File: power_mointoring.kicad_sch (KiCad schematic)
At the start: 19 parts, among them J10 BATT out, J11 Vin, J7 VCC, J8 Servo pwr, J9 BATT in, SW5 POWER, U3 3V3 REG, U4 DS2438Z+, U5 DS2438Z+

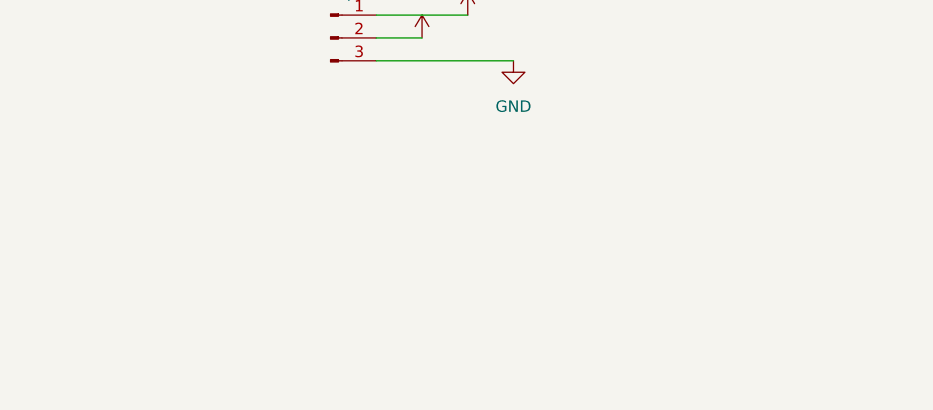
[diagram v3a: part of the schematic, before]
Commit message: Added revision 2 features, not routed.
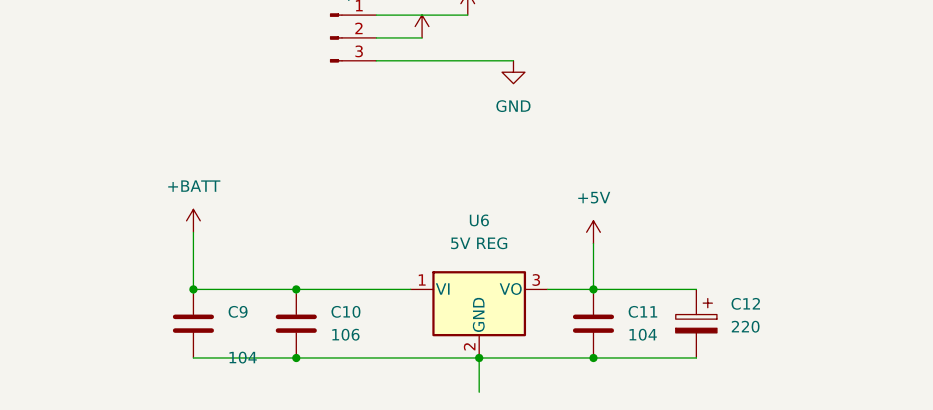
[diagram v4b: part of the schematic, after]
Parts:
- added C10: 106, Capacitor_SMD:C_1210_3225Metric_Pad1.33x2.70mm_HandSolder, symbol Device:C
- added C11, C9: 104, Capacitor_SMD:C_1206_3216Metric_Pad1.33x1.80mm_HandSolder, symbol Device:C
- added C12: 220, Capacitor_SMD:C_Elec_6.3x5.8, symbol Device:C_Polarized
- added U6: 5V REG, Package_TO_SOT_THT:TO-220-3_Vertical, symbol Regulator_Linear:LT1584-3.3
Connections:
- net +5V: now also C11.1, C12.1, U6.3 (VO)
- net +BATT: now also C10.1, C9.1, U6.1 (VI)
- new net: C10.2, C11.2, C12.2, C9.2, U6.2 (GND)
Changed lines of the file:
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@@
     (company "James Hudson")
   )
+  (junction (at 66.04 180.34) (diameter 0) (color 0 0 0 0)
+  )
   (junction (at 111.76 92.71) (diameter 0) (color 0 0 0 0)
   )
@@
   (junction (at 44.45 35.56) (diameter 0) (color 0 0 0 0)
   )
+  (junction (at 77.47 187.96) (diameter 0) (color 0 0 0 0)
+  )
   (junction (at 77.47 35.56) (diameter 0) (color 0 0 0 0)
   )
+  (junction (at 77.47 180.34) (diameter 0) (color 0 0 0 0)
+  )
+  (junction (at 97.79 187.96) (diameter 0) (color 0 0 0 0)
+  )
+  (junction (at 110.49 187.96) (diameter 0) (color 0 0 0 0)
+  )
   (junction (at 33.02 35.56) (diameter 0) (color 0 0 0 0)
   )
@@
   (junction (at 64.77 43.18) (diameter 0) (color 0 0 0 0)
   )
+  (junction (at 110.49 180.34) (diameter 0) (color 0 0 0 0)
+  )
   (wire (pts (xy 97.79 82.55) (xy 97.79 92.71))
     (stroke (width 0) (type default) (color 0 0 0 0))
@@
     (stroke (width 0) (type default) (color 0 0 0 0))
   )
+  (wire (pts (xy 66.04 173.99) (xy 66.04 180.34))
+    (stroke (width 0) (type default) (color 0 0 0 0))
+  )
+  (wire (pts (xy 97.79 187.96) (xy 97.79 191.77))
+    (stroke (width 0) (type default) (color 0 0 0 0))
+  )
   (wire (pts (xy 194.31 116.84) (xy 199.39 116.84))
     (stroke (width 0) (type default) (color 0 0 0 0))
@@
     (stroke (width 0) (type default) (color 0 0 0 0))
   )
+  (wire (pts (xy 90.17 180.34) (xy 77.47 180.34))
+    (stroke (width 0) (type default) (color 0 0 0 0))
+  )
   (wire (pts (xy 149.86 72.39) (xy 149.86 77.47))
     (stroke (width 0) (type default) (color 0 0 0 0))
   )
+  (wire (pts (xy 110.49 175.26) (xy 110.49 180.34))
+    (stroke (width 0) (type default) (color 0 0 0 0))
+  )
   (wire (pts (xy 137.16 62.23) (xy 161.29 62.23))
     (stroke (width 0) (type default) (color 0 0 0 0))
@@
     (stroke (width 0) (type default) (color 0 0 0 0))
   )
+  (wire (pts (xy 110.49 187.96) (xy 121.92 187.96))
+    (stroke (width 0) (type default) (color 0 0 0 0))
+  )
   (wire (pts (xy 86.36 154.94) (xy 101.6 154.94))
     (stroke (width 0) (type default) (color 0 0 0 0))
@@
     (stroke (width 0) (type default) (color 0 0 0 0))
   )
+  (wire (pts (xy 110.49 180.34) (xy 121.92 180.34))
+    (stroke (width 0) (type default) (color 0 0 0 0))
+  )
   (wire (pts (xy 107.95 69.85) (xy 115.57 69.85))
     (stroke (width 0) (type default) (color 0 0 0 0))
@@
     (stroke (width 0) (type default) (color 0 0 0 0))
   )
+  (wire (pts (xy 105.41 180.34) (xy 110.49 180.34))
+    (stroke (width 0) (type default) (color 0 0 0 0))
+  )
   (wire (pts (xy 161.29 72.39) (xy 161.29 69.85))
     (stroke (width 0) (type default) (color 0 0 0 0))
@@
     (stroke (width 0) (type default) (color 0 0 0 0))
   )
+  (wire (pts (xy 97.79 187.96) (xy 110.49 187.96))
+    (stroke (width 0) (type default) (color 0 0 0 0))
+  )
   (wire (pts (xy 77.47 35.56) (xy 88.9 35.56))
     (stroke (width 0) (type default) (color 0 0 0 0))
@@
     (stroke (width 0) (type default) (color 0 0 0 0))
   )
+  (wire (pts (xy 66.04 180.34) (xy 77.47 180.34))
+    (stroke (width 0) (type default) (color 0 0 0 0))
+  )
   (wire (pts (xy 33.02 43.18) (xy 44.45 43.18))
     (stroke (width 0) (type default) (color 0 0 0 0))
@@
     (stroke (width 0) (type default) (color 0 0 0 0))
   )
+  (wire (pts (xy 77.47 187.96) (xy 97.79 187.96))
+    (stroke (width 0) (type default) (color 0 0 0 0))
+  )
   (wire (pts (xy 161.29 129.54) (xy 144.78 129.54))
     (stroke (width 0) (type default) (color 0 0 0 0))
@@
   )
   (wire (pts (xy 77.47 30.48) (xy 77.47 35.56))
+    (stroke (width 0) (type default) (color 0 0 0 0))
+  )
+  (wire (pts (xy 66.04 187.96) (xy 77.47 187.96))
     (stroke (width 0) (type default) (color 0 0 0 0))
   )
@@
     (pin "2")
     (pin "3")
+  )
+  (symbol (lib_id "Device:C") (at 66.04 184.15 0) (unit 1)
+    (in_bom yes) (on_board yes)
+    (property "Reference" "C9" (id 0) (at 69.85 182.8799 0)
+      (effects (font (size 1.27 1.27)) (justify left))
+    )
+    (property "Value" "104" (id 1) (at 69.85 187.96 0)
+      (effects (font (size 1.27 1.27)) (justify left))
+    )
+    (property "Footprint" "Capacitor_SMD:C_1206_3216Metric_Pad1.33x1.80mm_HandSolder" (id 2) (at 67.0052 187.96 0)
+      (effects (font (size 1.27 1.27)) hide)
+    )
+    (property "Datasheet" "~" (id 3) (at 66.04 184.15 0)
+      (effects (font (size 1.27 1.27)) hide)
+    )
+    (pin "1")
+    (pin "2")
   )
   (symbol (lib_id "Switch:SW_SPDT") (at 120.65 72.39 0) (mirror y) (unit 1)
@@
     (pin "2")
   )
+  (symbol (lib_id "Device:C") (at 77.47 184.15 0) (unit 1)
+    (in_bom yes) (on_board yes) (fields_autoplaced)
+    (property "Reference" "C10" (id 0) (at 81.28 182.8799 0)
+      (effects (font (size 1.27 1.27)) (justify left))
+    )
+    (property "Value" "106" (id 1) (at 81.28 185.4199 0)
+      (effects (font (size 1.27 1.27)) (justify left))
+    )
+    (property "Footprint" "Capacitor_SMD:C_1210_3225Metric_Pad1.33x2.70mm_HandSolder" (id 2) (at 78.4352 187.96 0)
+      (effects (font (size 1.27 1.27)) hide)
+    )
+    (property "Datasheet" "~" (id 3) (at 77.47 184.15 0)
+      (effects (font (size 1.27 1.27)) hide)
+    )
+    (pin "1")
+    (pin "2")
+  )
   (symbol (lib_id "Connector:Conn_01x02_Male") (at 48.26 111.76 0) (unit 1)
     (in_bom yes) (on_board yes) (fields_autoplaced)
@@
     )
     (property "Datasheet" "https://www.analog.com/media/en/technical-documentation/data-sheets/158457a.pdf" (id 3) (at 64.77 57.15 0)
+      (effects (font (size 1.27 1.27)) hide)
+    )
+    (pin "1")
+    (pin "2")
+    (pin "3")
+  )
+  (symbol (lib_id "Regulator_Linear:LT1584-3.3") (at 97.79 180.34 0) (unit 1)
+    (in_bom yes) (on_board yes) (fields_autoplaced)
+    (property "Reference" "U6" (id 0) (at 97.79 172.72 0))
+    (property "Value" "5V REG" (id 1) (at 97.79 175.26 0))
+    (property "Footprint" "Package_TO_SOT_THT:TO-220-3_Vertical" (id 2) (at 97.79 173.99 0)
+      (effects (font (size 1.27 1.27) italic) hide)
+    )
+    (property "Datasheet" "https://www.analog.com/media/en/technical-documentation/data-sheets/158457a.pdf" (id 3) (at 97.79 201.93 0)
       (effects (font (size 1.27 1.27)) hide)
     )
@@
     (pin "8")
   )
+  (symbol (lib_id "power:+BATT") (at 66.04 173.99 0) (unit 1)
+    (in_bom yes) (on_board yes) (fields_autoplaced)
+    (property "Reference" "#PWR0115" (id 0) (at 66.04 177.8 0)
+      (effects (font (size 1.27 1.27)) hide)
+    )
+    (property "Value" "+BATT" (id 1) (at 66.04 168.91 0))
+    (property "Footprint" "" (id 2) (at 66.04 173.99 0)
+      (effects (font (size 1.27 1.27)) hide)
+    )
+    (property "Datasheet" "" (id 3) (at 66.04 173.99 0)
+      (effects (font (size 1.27 1.27)) hide)
+    )
+    (pin "1")
+  )
   (symbol (lib_id "power:VCC") (at 152.4 116.84 0) (unit 1)
     (in_bom yes) (on_board yes) (fields_autoplaced)
@@
     )
     (property "Datasheet" "" (id 3) (at 152.4 116.84 0)
+      (effects (font (size 1.27 1.27)) hide)
+    )
+    (pin "1")
+  )
+  (symbol (lib_id "Device:C") (at 110.49 184.15 0) (unit 1)
+    (in_bom yes) (on_board yes) (fields_autoplaced)
+    (property "Reference" "C11" (id 0) (at 114.3 182.8799 0)
+      (effects (font (size 1.27 1.27)) (justify left))
+    )
+    (property "Value" "104" (id 1) (at 114.3 185.4199 0)
+      (effects (font (size 1.27 1.27)) (justify left))
+    )
+    (property "Footprint" "Capacitor_SMD:C_1206_3216Metric_Pad1.33x1.80mm_HandSolder" (id 2) (at 111.4552 187.96 0)
+      (effects (font (size 1.27 1.27)) hide)
+    )
+    (property "Datasheet" "~" (id 3) (at 110.49 184.15 0)
+      (effects (font (size 1.27 1.27)) hide)
+    )
+    (pin "1")
+    (pin "2")
+  )
+  (symbol (lib_id "power:+5V") (at 110.49 175.26 0) (unit 1)
+    (in_bom yes) (on_board yes) (fields_autoplaced)
+    (property "Reference" "#PWR0114" (id 0) (at 110.49 179.07 0)
+      (effects (font (size 1.27 1.27)) hide)
+    )
+    (property "Value" "+5V" (id 1) (at 110.49 170.18 0))
+    (property "Footprint" "" (id 2) (at 110.49 175.26 0)
+      (effects (font (size 1.27 1.27)) hide)
+    )
+    (property "Datasheet" "" (id 3) (at 110.49 175.26 0)
       (effects (font (size 1.27 1.27)) hide)
     )
@@
     (pin "1")
   )
+  (symbol (lib_id "Device:C_Polarized") (at 121.92 184.15 0) (mirror y) (unit 1)
+    (in_bom yes) (on_board yes) (fields_autoplaced)
+    (property "Reference" "C12" (id 0) (at 125.73 181.9909 0)
+      (effects (font (size 1.27 1.27)) (justify right))
+    )
+    (property "Value" "220" (id 1) (at 125.73 184.5309 0)
+      (effects (font (size 1.27 1.27)) (justify right))
+    )
+    (property "Footprint" "Capacitor_SMD:C_Elec_6.3x5.8" (id 2) (at 120.9548 187.96 0)
+      (effects (font (size 1.27 1.27)) hide)
+    )
+    (property "Datasheet" "~" (id 3) (at 121.92 184.15 0)
+      (effects (font (size 1.27 1.27)) hide)
+    )
+    (pin "1")
+    (pin "2")
+  )
   (symbol (lib_id "power:+BATT") (at 133.35 72.39 0) (unit 1)

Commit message: Board ready to go.
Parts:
- removed J10: BATT out, Connector_PinHeader_2.54mm:Connector_Battery_SolderPads, symbol Connector:Conn_01x02_Male
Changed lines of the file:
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@@
-    (stroke (width 0) (type default) (color 0 0 0 0))
-  )
-  (wire (pts (xy 99.06 121.92) (xy 104.14 121.92))
     (stroke (width 0) (type default) (color 0 0 0 0))
   )
@@
   )
   (wire (pts (xy 194.31 109.22) (xy 194.31 116.84))
-    (stroke (width 0) (type default) (color 0 0 0 0))
-  )
-  (wire (pts (xy 99.06 119.38) (xy 104.14 119.38))
     (stroke (width 0) (type default) (color 0 0 0 0))
   )
@@
     (pin "2")
   )
-  (symbol (lib_id "power:+BATT") (at 104.14 119.38 0) (unit 1)
-    (in_bom yes) (on_board yes)
-    (property "Reference" "#PWR067" (id 0) (at 104.14 123.19 0)
-      (effects (font (size 1.27 1.27)) hide)
-    )
-    (property "Value" "+BATT" (id 1) (at 104.14 114.3 0))
-    (property "Footprint" "" (id 2) (at 104.14 119.38 0)
-      (effects (font (size 1.27 1.27)) hide)
-    )
-    (property "Datasheet" "" (id 3) (at 104.14 119.38 0)
-      (effects (font (size 1.27 1.27)) hide)
-    )
-    (pin "1")
-  )
   (symbol (lib_id "power:GND") (at 153.67 92.71 0) (unit 1)
     (in_bom yes) (on_board yes) (fields_autoplaced)
@@
     (pin "1")
     (pin "2")
-  )
-  (symbol (lib_id "power:GND") (at 104.14 121.92 0) (unit 1)
-    (in_bom yes) (on_board yes) (fields_autoplaced)
-    (property "Reference" "#PWR068" (id 0) (at 104.14 128.27 0)
-      (effects (font (size 1.27 1.27)) hide)
-    )
-    (property "Value" "GND" (id 1) (at 104.14 127 0))
-    (property "Footprint" "" (id 2) (at 104.14 121.92 0)
-      (effects (font (size 1.27 1.27)) hide)
-    )
-    (property "Datasheet" "" (id 3) (at 104.14 121.92 0)
-      (effects (font (size 1.27 1.27)) hide)
-    )
-    (pin "1")
   )
   (symbol (lib_id "Device:C") (at 77.47 39.37 0) (unit 1)
@@
     (pin "1")
   )
-  (symbol (lib_id "Connector:Conn_01x02_Male") (at 93.98 119.38 0) (unit 1)
-    (in_bom yes) (on_board yes) (fields_autoplaced)
-    (property "Reference" "J10" (id 0) (at 94.615 114.3 0))
-    (property "Value" "BATT out" (id 1) (at 94.615 116.84 0))
-    (property "Footprint" "Connector_PinHeader_2.54mm:Connector_Battery_SolderPads" (id 2) (at 93.98 119.38 0)
-      (effects (font (size 1.27 1.27)) hide)
-    )
-    (property "Datasheet" "~" (id 3) (at 93.98 119.38 0)
-      (effects (font (size 1.27 1.27)) hide)
-    )
-    (pin "1")
-    (pin "2")
-  )
   (symbol (lib_id "Device:R") (at 149.86 81.28 0) (unit 1)

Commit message: Clean chematic
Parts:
- added J10: Servo pwr, Connector_PinHeader_2.54mm:Connector_SolderPadsx3, symbol Connector:Conn_01x03_Male
- added J13: VCC, Connector_PinHeader_2.54mm:PinHeader_1x02_P2.54mm_Vertical, symbol Connector:Conn_01x02_Male
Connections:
- net +5V: no longer U4.4 (VAD)
- net GND: now also J10.3 (Pin_3), J13.2 (Pin_2)
- net VCC: now also J13.1 (Pin_1)
- new net +5VA: J10.1 (Pin_1)
- new net +5VL: J10.2 (Pin_2), U4.4 (VAD)
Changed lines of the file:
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@@
+    (stroke (width 0) (type default) (color 0 0 0 0))
+  )
+  (wire (pts (xy 53.34 132.08) (xy 58.42 132.08))
     (stroke (width 0) (type default) (color 0 0 0 0))
   )
@@
     (stroke (width 0) (type default) (color 0 0 0 0))
   )
+  (wire (pts (xy 133.35 154.94) (xy 148.59 154.94))
+    (stroke (width 0) (type default) (color 0 0 0 0))
+  )
   (wire (pts (xy 97.79 187.96) (xy 97.79 191.77))
     (stroke (width 0) (type default) (color 0 0 0 0))
   )
+  (wire (pts (xy 53.34 134.62) (xy 58.42 134.62))
+    (stroke (width 0) (type default) (color 0 0 0 0))
+  )
   (wire (pts (xy 194.31 116.84) (xy 199.39 116.84))
     (stroke (width 0) (type default) (color 0 0 0 0))
@@
     (stroke (width 0) (type default) (color 0 0 0 0))
   )
+  (wire (pts (xy 133.35 149.86) (xy 143.51 149.86))
+    (stroke (width 0) (type default) (color 0 0 0 0))
+  )
   (wire (pts (xy 189.23 69.85) (xy 189.23 76.2))
     (stroke (width 0) (type default) (color 0 0 0 0))
@@
   )
   (wire (pts (xy 161.29 129.54) (xy 144.78 129.54))
+    (stroke (width 0) (type default) (color 0 0 0 0))
+  )
+  (wire (pts (xy 133.35 152.4) (xy 147.32 152.4))
     (stroke (width 0) (type default) (color 0 0 0 0))
   )
@@
     (pin "2")
   )
+  (symbol (lib_id "power:VCC") (at 58.42 132.08 0) (unit 1)
+    (in_bom yes) (on_board yes) (fields_autoplaced)
+    (property "Reference" "#PWR0178" (id 0) (at 58.42 135.89 0)
+      (effects (font (size 1.27 1.27)) hide)
+    )
+    (property "Value" "VCC" (id 1) (at 58.42 127 0))
+    (property "Footprint" "" (id 2) (at 58.42 132.08 0)
+      (effects (font (size 1.27 1.27)) hide)
+    )
+    (property "Datasheet" "" (id 3) (at 58.42 132.08 0)
+      (effects (font (size 1.27 1.27)) hide)
+    )
+    (pin "1")
+  )
   (symbol (lib_id "Connector:Conn_01x02_Male") (at 92.71 80.01 0) (unit 1)
     (in_bom yes) (on_board yes) (fields_autoplaced)
@@
     (pin "1")
   )
+  (symbol (lib_id "power:GND") (at 58.42 134.62 0) (unit 1)
+    (in_bom yes) (on_board yes) (fields_autoplaced)
+    (property "Reference" "#PWR0176" (id 0) (at 58.42 140.97 0)
+      (effects (font (size 1.27 1.27)) hide)
+    )
+    (property "Value" "GND" (id 1) (at 58.42 139.7 0))
+    (property "Footprint" "" (id 2) (at 58.42 134.62 0)
+      (effects (font (size 1.27 1.27)) hide)
+    )
+    (property "Datasheet" "" (id 3) (at 58.42 134.62 0)
+      (effects (font (size 1.27 1.27)) hide)
+    )
+    (pin "1")
+  )
+  (symbol (lib_id "power:GND") (at 148.59 154.94 0) (unit 1)
+    (in_bom yes) (on_board yes) (fields_autoplaced)
+    (property "Reference" "#PWR0157" (id 0) (at 148.59 161.29 0)
+      (effects (font (size 1.27 1.27)) hide)
+    )
+    (property "Value" "GND" (id 1) (at 148.59 160.02 0))
+    (property "Footprint" "" (id 2) (at 148.59 154.94 0)
+      (effects (font (size 1.27 1.27)) hide)
+    )
+    (property "Datasheet" "" (id 3) (at 148.59 154.94 0)
+      (effects (font (size 1.27 1.27)) hide)
+    )
+    (pin "1")
+  )
   (symbol (lib_id "Device:C") (at 143.51 72.39 270) (unit 1)
     (in_bom yes) (on_board yes) (fields_autoplaced)
@@
     (pin "1")
   )
+  (symbol (lib_id "Connector:Conn_01x02_Male") (at 48.26 132.08 0) (unit 1)
+    (in_bom yes) (on_board yes) (fields_autoplaced)
+    (property "Reference" "J13" (id 0) (at 48.895 127 0))
+    (property "Value" "VCC" (id 1) (at 48.895 129.54 0))
+    (property "Footprint" "Connector_PinHeader_2.54mm:PinHeader_1x02_P2.54mm_Vertical" (id 2) (at 48.26 132.08 0)
+      (effects (font (size 1.27 1.27)) hide)
+    )
+    (property "Datasheet" "~" (id 3) (at 48.26 132.08 0)
+      (effects (font (size 1.27 1.27)) hide)
+    )
+    (pin "1")
+    (pin "2")
+  )
   (symbol (lib_id "Device:Fuse") (at 104.14 69.85 270) (unit 1)
     (in_bom yes) (on_board yes) (fields_autoplaced)
@@
     (pin "1")
     (pin "2")
+  )
+  (symbol (lib_id "power:+5VA") (at 143.51 149.86 0) (unit 1)
+    (in_bom yes) (on_board yes) (fields_autoplaced)
+    (property "Reference" "#PWR0154" (id 0) (at 143.51 153.67 0)
+      (effects (font (size 1.27 1.27)) hide)
+    )
+    (property "Value" "+5VA" (id 1) (at 143.51 144.78 0))
+    (property "Footprint" "" (id 2) (at 143.51 149.86 0)
+      (effects (font (size 1.27 1.27)) hide)
+    )
+    (property "Datasheet" "" (id 3) (at 143.51 149.86 0)
+      (effects (font (size 1.27 1.27)) hide)
+    )
+    (pin "1")
   )
   (symbol (lib_id "Device:C") (at 77.47 39.37 0) (unit 1)
@@
     (pin "1")
   )
-  (symbol (lib_id "power:+5V") (at 156.21 72.39 0) (unit 1)
-    (in_bom yes) (on_board yes) (fields_autoplaced)
-    (property "Reference" "#PWR073" (id 0) (at 156.21 76.2 0)
-      (effects (font (size 1.27 1.27)) hide)
-    )
-    (property "Value" "+5V" (id 1) (at 156.21 67.31 0))
-    (property "Footprint" "" (id 2) (at 156.21 72.39 0)
-      (effects (font (size 1.27 1.27)) hide)
-    )
-    (property "Datasheet" "" (id 3) (at 156.21 72.39 0)
-      (effects (font (size 1.27 1.27)) hide)
-    )
-    (pin "1")
-  )
   (symbol (lib_id "power:+5V") (at 96.52 149.86 0) (unit 1)
     (in_bom yes) (on_board yes) (fields_autoplaced)
@@
     )
     (property "Datasheet" "" (id 3) (at 96.52 149.86 0)
+      (effects (font (size 1.27 1.27)) hide)
+    )
+    (pin "1")
+  )
+  (symbol (lib_id "power:+5VL") (at 147.32 152.4 0) (unit 1)
+    (in_bom yes) (on_board yes) (fields_autoplaced)
+    (property "Reference" "#PWR0166" (id 0) (at 147.32 156.21 0)
+      (effects (font (size 1.27 1.27)) hide)
+    )
+    (property "Value" "+5VL" (id 1) (at 147.32 147.32 0))
+    (property "Footprint" "" (id 2) (at 147.32 152.4 0)
+      (effects (font (size 1.27 1.27)) hide)
+    )
+    (property "Datasheet" "" (id 3) (at 147.32 152.4 0)
+      (effects (font (size 1.27 1.27)) hide)
+    )
+    (pin "1")
+  )
+  (symbol (lib_id "power:+5VL") (at 156.21 72.39 0) (unit 1)
+    (in_bom yes) (on_board yes) (fields_autoplaced)
+    (property "Reference" "#PWR0172" (id 0) (at 156.21 76.2 0)
+      (effects (font (size 1.27 1.27)) hide)
+    )
+    (property "Value" "+5VL" (id 1) (at 156.21 67.31 0))
+    (property "Footprint" "" (id 2) (at 156.21 72.39 0)
+      (effects (font (size 1.27 1.27)) hide)
+    )
+    (property "Datasheet" "" (id 3) (at 156.21 72.39 0)
       (effects (font (size 1.27 1.27)) hide)
     )
@@
     (pin "1")
   )
+  (symbol (lib_id "Connector:Conn_01x03_Male") (at 128.27 152.4 0) (unit 1)
+    (in_bom yes) (on_board yes) (fields_autoplaced)
+    (property "Reference" "J10" (id 0) (at 128.905 144.78 0))
+    (property "Value" "Servo pwr" (id 1) (at 128.905 147.32 0))
+    (property "Footprint" "Connector_PinHeader_2.54mm:Connector_SolderPadsx3" (id 2) (at 128.27 152.4 0)
+      (effects (font (size 1.27 1.27)) hide)
+    )
+    (property "Datasheet" "~" (id 3) (at 128.27 152.4 0)
+      (effects (font (size 1.27 1.27)) hide)
+    )
+    (pin "1")
+    (pin "2")
+    (pin "3")
+  )
   (symbol (lib_id "DS2438:DS2438Z+") (at 158.75 57.15 0) (unit 1)
